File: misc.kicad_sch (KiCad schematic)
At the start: 0 parts

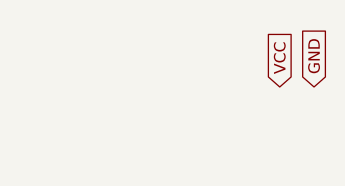
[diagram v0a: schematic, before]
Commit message: now using correct VCC and GND symbols
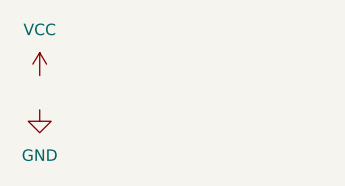
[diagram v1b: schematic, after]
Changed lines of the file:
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@@
 (kicad_sch (version 20211123) (generator eeschema)
   (paper "A4")
-  (global_label "GND" (shape input) (at 64.77 34.29 90) (fields_autoplaced)
-    (effects (font (size 1.27 1.27)) (justify left))
-    (property "Intersheet References" "${INTERSHEET_REFS}" (id 0) (at 64.6906 28.0064 90)
-      (effects (font (size 1.27 1.27)) (justify left) hide)
+  (symbol (lib_id "power:VCC") (at 34.29 33.02 0) (unit 1)
+    (in_bom yes) (on_board yes) (fields_autoplaced)
+    (property "Reference" "#PWR?" (id 0) (at 34.29 36.83 0)
+      (effects (font (size 1.27 1.27)) hide)
     )
+    (property "Value" "VCC" (id 1) (at 34.29 27.94 0))
+    (property "Footprint" "" (id 2) (at 34.29 33.02 0)
+      (effects (font (size 1.27 1.27)) hide)
+    )
+    (property "Datasheet" "" (id 3) (at 34.29 33.02 0)
+      (effects (font (size 1.27 1.27)) hide)
+    )
+    (pin "1")
   )
-  (global_label "VCC" (shape input) (at 60.96 34.29 90) (fields_autoplaced)
-    (effects (font (size 1.27 1.27)) (justify left))
-    (property "Intersheet References" "${INTERSHEET_REFS}" (id 0) (at 60.8806 28.2483 90)
-      (effects (font (size 1.27 1.27)) (justify left) hide)
+  (symbol (lib_id "power:GND") (at 34.29 36.83 0) (unit 1)
+    (in_bom yes) (on_board yes) (fields_autoplaced)
+    (property "Reference" "#PWR?" (id 0) (at 34.29 43.18 0)
+      (effects (font (size 1.27 1.27)) hide)
     )
+    (property "Value" "GND" (id 1) (at 34.29 41.91 0))
+    (property "Footprint" "" (id 2) (at 34.29 36.83 0)
+      (effects (font (size 1.27 1.27)) hide)
+    )
+    (property "Datasheet" "" (id 3) (at 34.29 36.83 0)
+      (effects (font (size 1.27 1.27)) hide)
+    )
+    (pin "1")
   )
 )

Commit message: added esp32 schematic && updated supply symbols
Signed-off-by: Tobias Gent <gent.tobias@gmail.com>
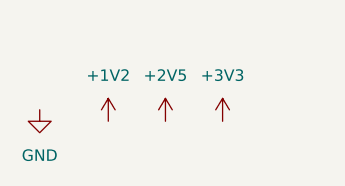
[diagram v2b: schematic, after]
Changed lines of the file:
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@@
 (kicad_sch (version 20211123) (generator eeschema)
   (paper "A4")
-  (symbol (lib_id "power:VCC") (at 34.29 33.02 0) (unit 1)
+  (symbol (lib_id "power:+1V2") (at 41.91 38.1 0) (unit 1)
     (in_bom yes) (on_board yes) (fields_autoplaced)
-    (property "Reference" "#PWR?" (id 0) (at 34.29 36.83 0)
+    (property "Reference" "#PWR?" (id 0) (at 41.91 41.91 0)
       (effects (font (size 1.27 1.27)) hide)
     )
-    (property "Value" "VCC" (id 1) (at 34.29 27.94 0))
-    (property "Footprint" "" (id 2) (at 34.29 33.02 0)
+    (property "Value" "+1V2" (id 1) (at 41.91 33.02 0))
+    (property "Footprint" "" (id 2) (at 41.91 38.1 0)
       (effects (font (size 1.27 1.27)) hide)
     )
-    (property "Datasheet" "" (id 3) (at 34.29 33.02 0)
+    (property "Datasheet" "" (id 3) (at 41.91 38.1 0)
       (effects (font (size 1.27 1.27)) hide)
     )
+    (pin "1")
+  )
+  (symbol (lib_id "power:+2V5") (at 48.26 38.1 0) (unit 1)
+    (in_bom yes) (on_board yes) (fields_autoplaced)
+    (property "Reference" "#PWR?" (id 0) (at 48.26 41.91 0)
+      (effects (font (size 1.27 1.27)) hide)
+    )
+    (property "Value" "+2V5" (id 1) (at 48.26 33.02 0))
+    (property "Footprint" "" (id 2) (at 48.26 38.1 0)
+      (effects (font (size 1.27 1.27)) hide)
+    )
+    (property "Datasheet" "" (id 3) (at 48.26 38.1 0)
+      (effects (font (size 1.27 1.27)) hide)
+    )
+    (pin "1")
+  )
+  (symbol (lib_id "power:+3V3") (at 54.61 38.1 0) (unit 1)
+    (in_bom yes) (on_board yes) (fields_autoplaced)
+    (property "Reference" "#PWR?" (id 0) (at 54.61 41.91 0)
+      (effects (font (size 1.27 1.27)) hide)
+    )
+    (property "Value" "+3V3" (id 1) (at 54.61 33.02 0))
+    (property "Footprint" "" (id 2) (at 54.61 38.1 0)
+      (effects (font (size 1.27 1.27)) hide)
+    )
+    (property "Datasheet" "" (id 3) (at 54.61 38.1 0)
+      (effects (font (size 1.27 1.27)) hide)
+    )
